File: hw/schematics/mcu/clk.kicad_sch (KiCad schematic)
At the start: 9 parts

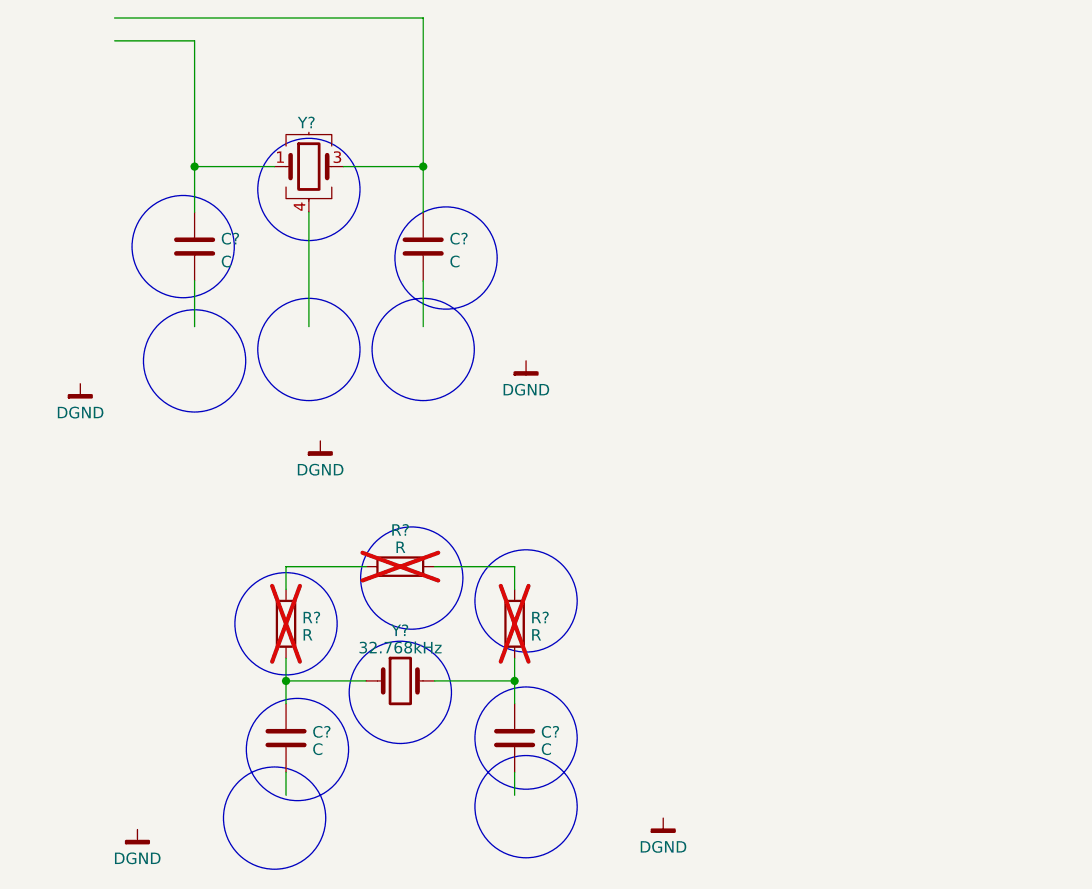
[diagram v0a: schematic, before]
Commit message: 
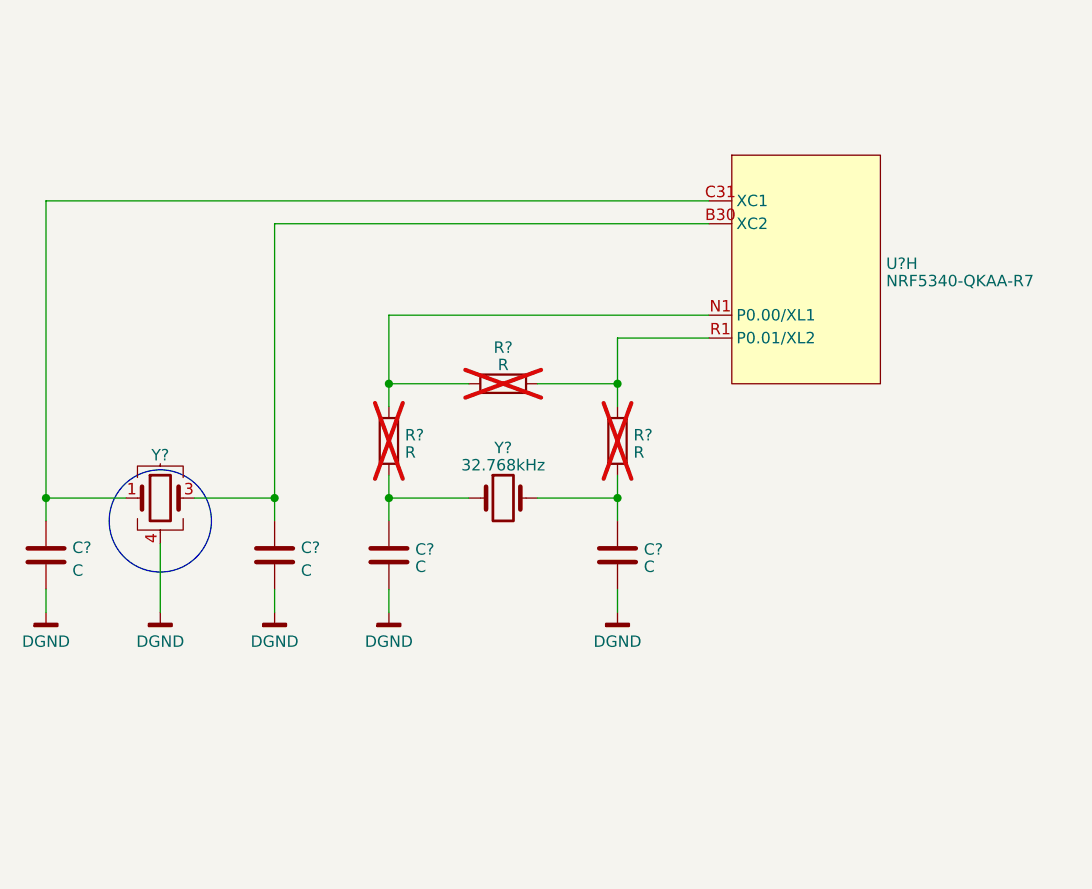
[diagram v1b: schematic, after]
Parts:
- added U?: NRF5340-QKAA-R7, 0:NRF5340-QKAA-R7, symbol 1.Embedded.Specialized:NRF5340-QKAA-R7
- Y?: footprint (none) -> Crystal:Crystal_SMD_TXC_9HT11-2Pin_2.0x1.2mm
- Y?: footprint 1.Logic.Oscillators_Resonators:32MHz-ECS-320-8-37B2-7KM-TR -> Crystal:Crystal_SMD_2016-4Pin_2.0x1.6mm
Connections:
- net DGND: now also C?.2, C?.2, C?.2, C?.2, Y?.2, Y?.4
- net at C?.1, Y?.3: now also U?.B30 (XC2)
- net at R?.1, R?.2: now also U?.N1 (P0.00/XL1)
- net at R?.2, R?.2: now also U?.R1 (P0.01/XL2)
- net at C?.1, Y?.1: now also U?.C31 (XC1)
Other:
- moved on the sheet: C?, R?, Y?
